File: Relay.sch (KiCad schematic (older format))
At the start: 0 parts

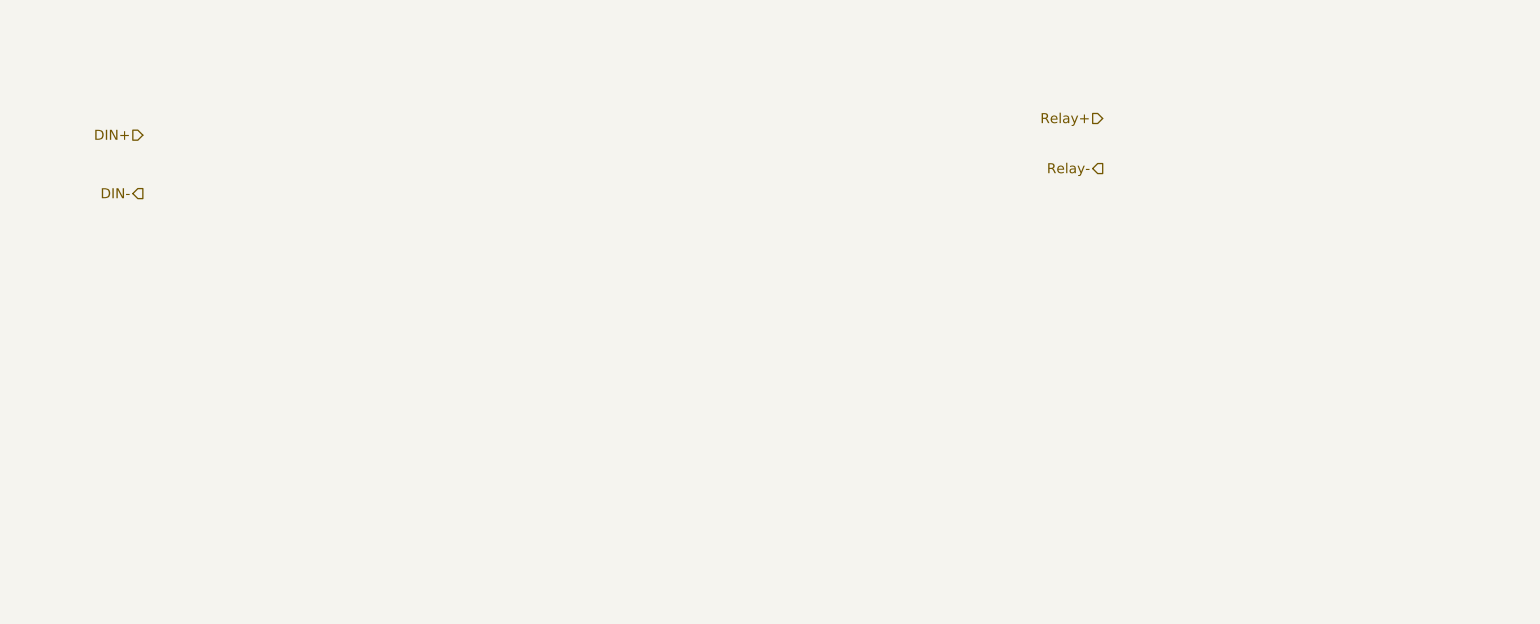
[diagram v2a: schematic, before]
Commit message: Initial Relay Module Schematic Wire Up
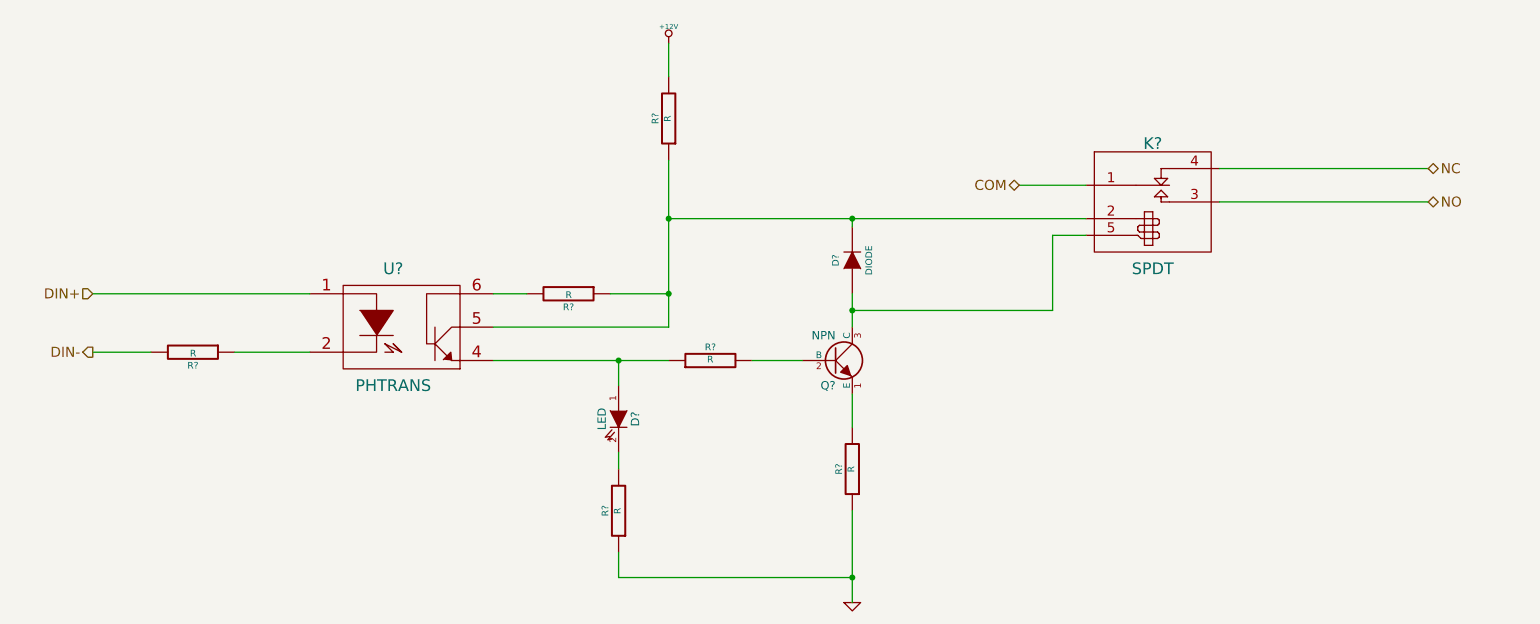
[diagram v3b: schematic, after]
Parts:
- added D?: LED, ~, symbol LED
- added D?: DIODE, ~, symbol DIODE
- added K?: SPDT, ~, symbol SPDT
- added Q?: NPN, ~, symbol NPN
- added R? (x6): R, ~, symbol R
- added U?: PHTRANS, ~, symbol PHTRANS
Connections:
- net DIN+: now also U?.1
- net DIN-: now also R?.2
- new net: R?.1, U?.2
- new net: D?.1 (A), R?.1, U?.4
- new net: D?.2 (K), K?.2 (COIL+), R?.1, R?.1, U?.5
- new net: R?.2, U?.6
- new net: D?.2 (K), R?.2
- new net: Q?.1 (E), R?.2
- new net: Q?.2 (B), R?.2
- new net: D?.1 (A), K?.5 (COIL-), Q?.3 (C)
- new net +12V: R?.2
- new net COM: K?.1 (COM)
- new net GND: R?.1, R?.1
- new net NC: K?.4 (NC)
- new net NO: K?.3 (NO)
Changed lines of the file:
@@
 LIBS:contrib
 LIBS:valves
+LIBS:BenchBudeeLib
 LIBS:BenchBudEE-cache
 EELAYER 27 0
@@
 Comment4 ""
 $EndDescr
-Text HLabel 2600 2450 0    60   Input ~ 0
+Text HLabel 2300 3400 0    60   Input ~ 0
 DIN+
-Text HLabel 2600 2800 0    60   Output ~ 0
+Text HLabel 2300 3750 0    60   Output ~ 0
 DIN-
-Text HLabel 8350 2350 0    60   Input ~ 0
-Relay+
-Text HLabel 8350 2650 0    60   Output ~ 0
-Relay-
+Text HLabel 10300 2650 2    60   BiDi ~ 0
+NC
+Text HLabel 10300 2850 2    60   BiDi ~ 0
+NO
+$Comp
+L PHTRANS U?
+U 1 1 52F1AD9F
+P 4150 3600
+F 0 "U?" H 4100 3950 70  0000 C CNN
+F 1 "PHTRANS" H 4100 3250 70  0000 C CNN
+F 2 "~" H 4150 3600 60  0000 C CNN
+F 3 "~" H 4150 3600 60  0000 C CNN
+	1    4150 3600
+	1    0    0    -1
+$EndComp
+$Comp
+L LED D?
+U 1 1 52F1ADBD
+P 5450 4150
+F 0 "D?" H 5450 4250 50  0000 C CNN
+F 1 "LED" H 5450 4050 50  0000 C CNN
+F 2 "~" H 5450 4150 60  0000 C CNN
+F 3 "~" H 5450 4150 60  0000 C CNN
+	1    5450 4150
+	0    1    1    0
+$EndComp
+$Comp
+L NPN Q?
+U 1 1 52F1ADCC
+P 6750 3800
+F 0 "Q?" H 6750 3650 50  0000 R CNN
+F 1 "NPN" H 6750 3950 50  0000 R CNN
+F 2 "~" H 6750 3800 60  0000 C CNN
+F 3 "~" H 6750 3800 60  0000 C CNN
+	1    6750 3800
+	1    0    0    -1
+$EndComp
+$Comp
+L SPDT K?
+U 1 1 52F1B21B
+P 8650 2700
+F 0 "K?" H 8650 2900 70  0000 C CNN
+F 1 "SPDT" H 8650 2150 70  0000 C CNN
+F 2 "~" H 8650 2700 60  0000 C CNN
+F 3 "~" H 8650 2700 60  0000 C CNN
+	1    8650 2700
+	1    0    0    -1
+$EndComp
+Text HLabel 7850 2750 0    60   BiDi ~ 0
+COM
+$Comp
+L R R?
+U 1 1 52F1B259
+P 6000 3800
+F 0 "R?" V 6080 3800 40  0000 C CNN
+F 1 "R" V 6007 3801 40  0000 C CNN
+F 2 "~" V 5930 3800 30  0000 C CNN
+F 3 "~" H 6000 3800 30  0000 C CNN
+	1    6000 3800
+	0    -1   -1   0
+$EndComp
+$Comp
+L R R?
+U 1 1 52F1B290
+P 6850 4450
+F 0 "R?" V 6930 4450 40  0000 C CNN
+F 1 "R" V 6857 4451 40  0000 C CNN
+F 2 "~" V 6780 4450 30  0000 C CNN
+F 3 "~" H 6850 4450 30  0000 C CNN
+	1    6850 4450
+	-1   0    0    1
+$EndComp
+$Comp
+L GND #PWR?
+U 1 1 52F1B29F
+P 6850 5250
+F 0 "#PWR?" H 6850 5250 30  0001 C CNN
+F 1 "GND" H 6850 5180 30  0001 C CNN
+F 2 "" H 6850 5250 60  0000 C CNN
+F 3 "" H 6850 5250 60  0000 C CNN
+	1    6850 5250
+	1    0    0    -1
+$EndComp
+$Comp
+L R R?
+U 1 1 52F1B2C7
+P 5450 4700
+F 0 "R?" V 5530 4700 40  0000 C CNN
+F 1 "R" V 5457 4701 40  0000 C CNN
+F 2 "~" V 5380 4700 30  0000 C CNN
+F 3 "~" H 5450 4700 30  0000 C CNN
+	1    5450 4700
+	-1   0    0    1
+$EndComp
+$Comp
+L R R?
+U 1 1 52F1B2D8
+P 5750 2350
+F 0 "R?" V 5830 2350 40  0000 C CNN
+F 1 "R" V 5757 2351 40  0000 C CNN
+F 2 "~" V 5680 2350 30  0000 C CNN
+F 3 "~" H 5750 2350 30  0000 C CNN
+	1    5750 2350
+	-1   0    0    1
+$EndComp
+$Comp
+L +12V #PWR?
+U 1 1 52F1B2E0
+P 5750 1900
+F 0 "#PWR?" H 5750 1850 20  0001 C CNN
+F 1 "+12V" H 5750 2000 30  0000 C CNN
+F 2 "" H 5750 1900 60  0000 C CNN
+F 3 "" H 5750 1900 60  0000 C CNN
+	1    5750 1900
+	1    0    0    -1
+$EndComp
+Wire Wire Line
+	7850 2750 8250 2750
+Wire Wire Line
+	9050 2650 10300 2650
+Wire Wire Line
+	10300 2850 9050 2850
+Wire Wire Line
+	4700 3800 5750 3800
+Wire Wire Line
+	6550 3800 6250 3800
+Wire Wire Line
+	6850 4000 6850 4200
+Wire Wire Line
+	6850 4700 6850 5250
+Wire Wire Line
+	5450 3800 5450 3950
+Connection ~ 5450 3800
+Wire Wire Line
+	5450 4350 5450 4450
+Wire Wire Line
+	5750 1900 5750 2100
+Wire Wire Line
+	5750 2950 8250 2950
+Wire Wire Line
+	5750 2600 5750 3600
+Wire Wire Line
+	6850 5100 5450 5100
+Wire Wire Line
+	5450 5100 5450 4950
+Connection ~ 6850 5100
+Wire Wire Line
+	5750 3600 4700 3600
+Connection ~ 5750 2950
+$Comp
+L R R?
+U 1 1 52F1B350
+P 5150 3400
+F 0 "R?" V 5230 3400 40  0000 C CNN
+F 1 "R" V 5157 3401 40  0000 C CNN
+F 2 "~" V 5080 3400 30  0000 C CNN
+F 3 "~" H 5150 3400 30  0000 C CNN
+	1    5150 3400
+	0    1    1    0
+$EndComp
+Wire Wire Line
+	4900 3400 4700 3400
+Wire Wire Line
+	5400 3400 5750 3400
+Connection ~ 5750 3400
+$Comp
+L R R?
+U 1 1 52F1B37F
+P 2900 3750
+F 0 "R?" V 2980 3750 40  0000 C CNN
+F 1 "R" V 2907 3751 40  0000 C CNN
+F 2 "~" V 2830 3750 30  0000 C CNN
+F 3 "~" H 2900 3750 30  0000 C CNN
+	1    2900 3750
+	0    1    1    0
+$EndComp
+Wire Wire Line
+	3150 3750 3600 3750
+Wire Wire Line
+	2300 3400 3600 3400
+Wire Wire Line
+	2300 3750 2650 3750
+$Comp
+L DIODE D?
+U 1 1 52F1B3D7
+P 6850 3200
+F 0 "D?" H 6850 3300 40  0000 C CNN
+F 1 "DIODE" H 6850 3100 40  0000 C CNN
+F 2 "~" H 6850 3200 60  0000 C CNN
+F 3 "~" H 6850 3200 60  0000 C CNN
+	1    6850 3200
+	0    -1   -1   0
+$EndComp
+Wire Wire Line
+	6850 3400 6850 3600
+Wire Wire Line
+	6850 3000 6850 2950
+Connection ~ 6850 2950
+Wire Wire Line
+	6850 3500 8050 3500
+Wire Wire Line
+	8050 3500 8050 3050
+Wire Wire Line
+	8050 3050 8250 3050
+Connection ~ 6850 3500
 $EndSCHEMATC

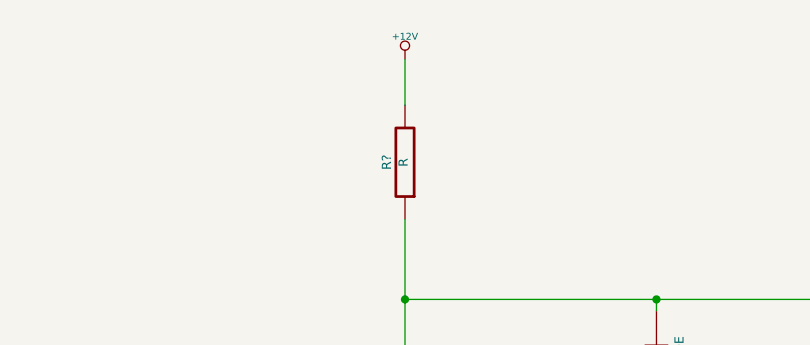
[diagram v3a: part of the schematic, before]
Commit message: Wire up Power Schematic
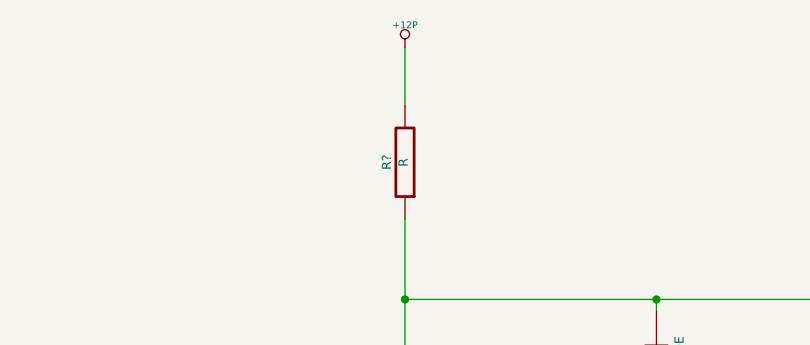
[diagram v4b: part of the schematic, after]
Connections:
- net +12V renamed +12P
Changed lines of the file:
@@
 $Descr A4 11693 8268
 encoding utf-8
-Sheet 3 8
+Sheet 3 9
 Title ""
 Date "5 feb 2014"
@@
 	-1   0    0    1
 $EndComp
-$Comp
-L +12V #PWR?
-U 1 1 52F1B2E0
-P 5750 1900
-F 0 "#PWR?" H 5750 1850 20  0001 C CNN
-F 1 "+12V" H 5750 2000 30  0000 C CNN
-F 2 "" H 5750 1900 60  0000 C CNN
-F 3 "" H 5750 1900 60  0000 C CNN
-	1    5750 1900
-	1    0    0    -1
-$EndComp
 Wire Wire Line
 	7850 2750 8250 2750
@@
 	5450 4350 5450 4450
 Wire Wire Line
-	5750 1900 5750 2100
+	5750 1850 5750 2100
 Wire Wire Line
 	5750 2950 8250 2950
@@
 	8050 3050 8250 3050
 Connection ~ 6850 3500
+$Comp
+L +12P #PWR?
+U 1 1 52F24BA2
+P 5750 1850
+F 0 "#PWR?" H 5750 1820 30  0001 C CNN
+F 1 "+12P" H 5750 1950 30  0000 C CNN
+F 2 "" H 5750 1850 60  0000 C CNN
+F 3 "" H 5750 1850 60  0000 C CNN
+	1    5750 1850
+	1    0    0    -1
+$EndComp
 $EndSCHEMATC

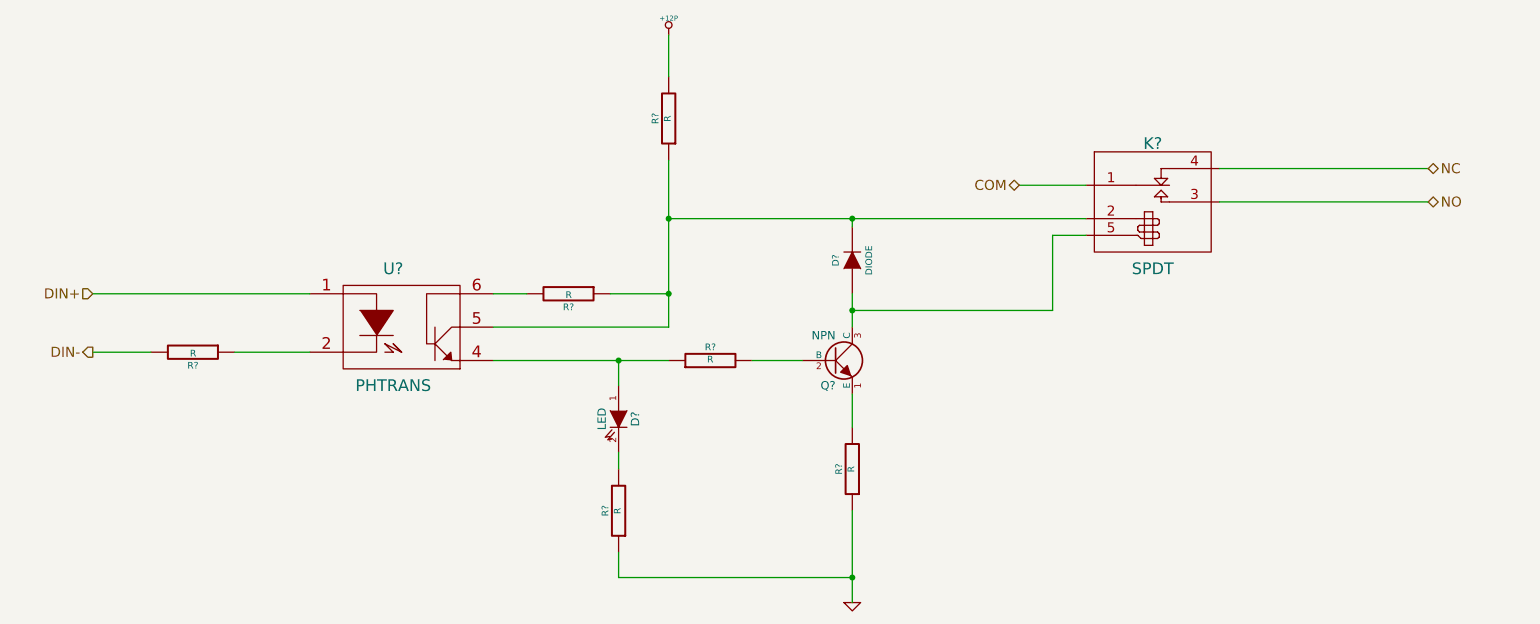
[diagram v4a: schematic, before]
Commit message: Create Arduino Schematic and Wire Up top Level
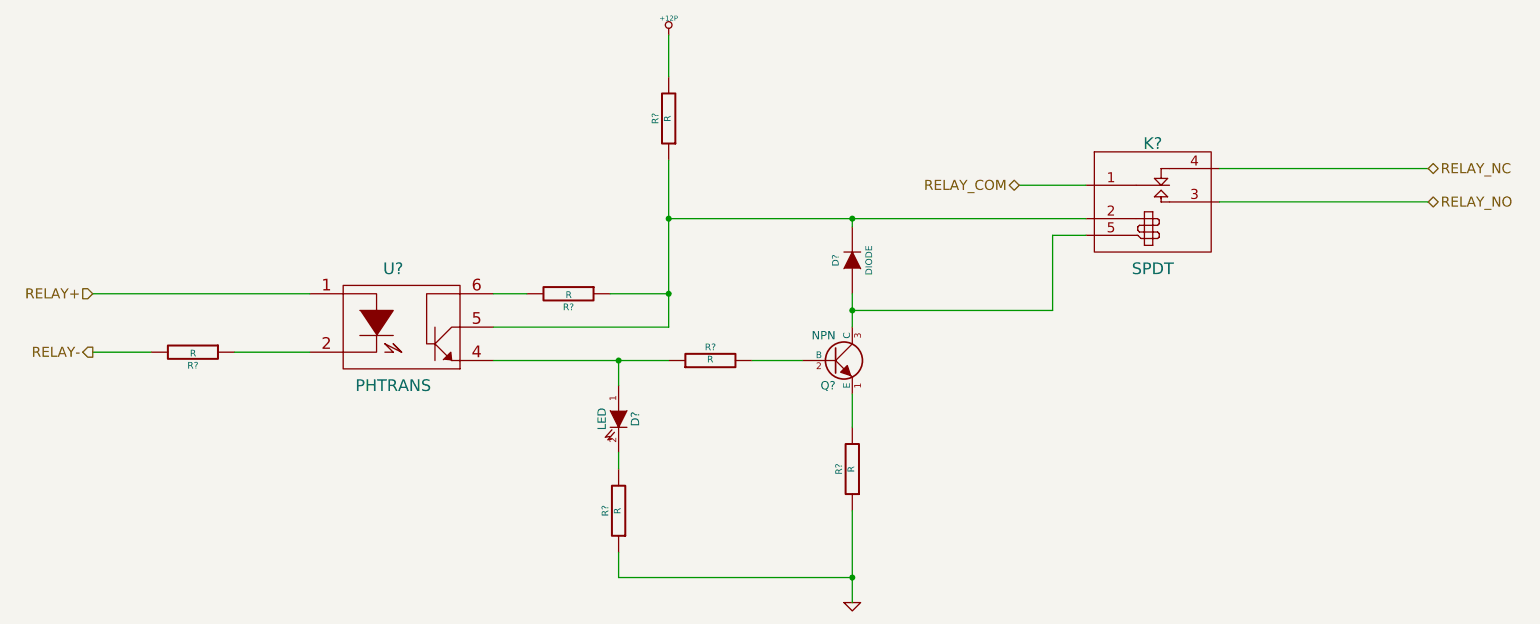
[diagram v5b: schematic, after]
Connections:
- net COM renamed RELAY_COM
- net DIN+ renamed RELAY+
- net DIN- renamed RELAY-
- net NC renamed RELAY_NC
- net NO renamed RELAY_NO
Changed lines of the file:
@@
 $EndDescr
 Text HLabel 2300 3400 0    60   Input ~ 0
-DIN+
+RELAY+
 Text HLabel 2300 3750 0    60   Output ~ 0
-DIN-
+RELAY-
 Text HLabel 10300 2650 2    60   BiDi ~ 0
-NC
+RELAY_NC
 Text HLabel 10300 2850 2    60   BiDi ~ 0
-NO
+RELAY_NO
 $Comp
 L PHTRANS U?
@@
 $EndComp
 Text HLabel 7850 2750 0    60   BiDi ~ 0
-COM
+RELAY_COM
 $Comp
 L R R?
